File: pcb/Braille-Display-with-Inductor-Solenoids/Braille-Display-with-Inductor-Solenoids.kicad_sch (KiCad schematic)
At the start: 18 parts, among them J1 Screw_Terminal_01x02, J2 Screw_Terminal_01x02, J3 Screw_Terminal_01x02, SW1 SW_Push, SW2 SW_Push, U1 RP2040-Zero

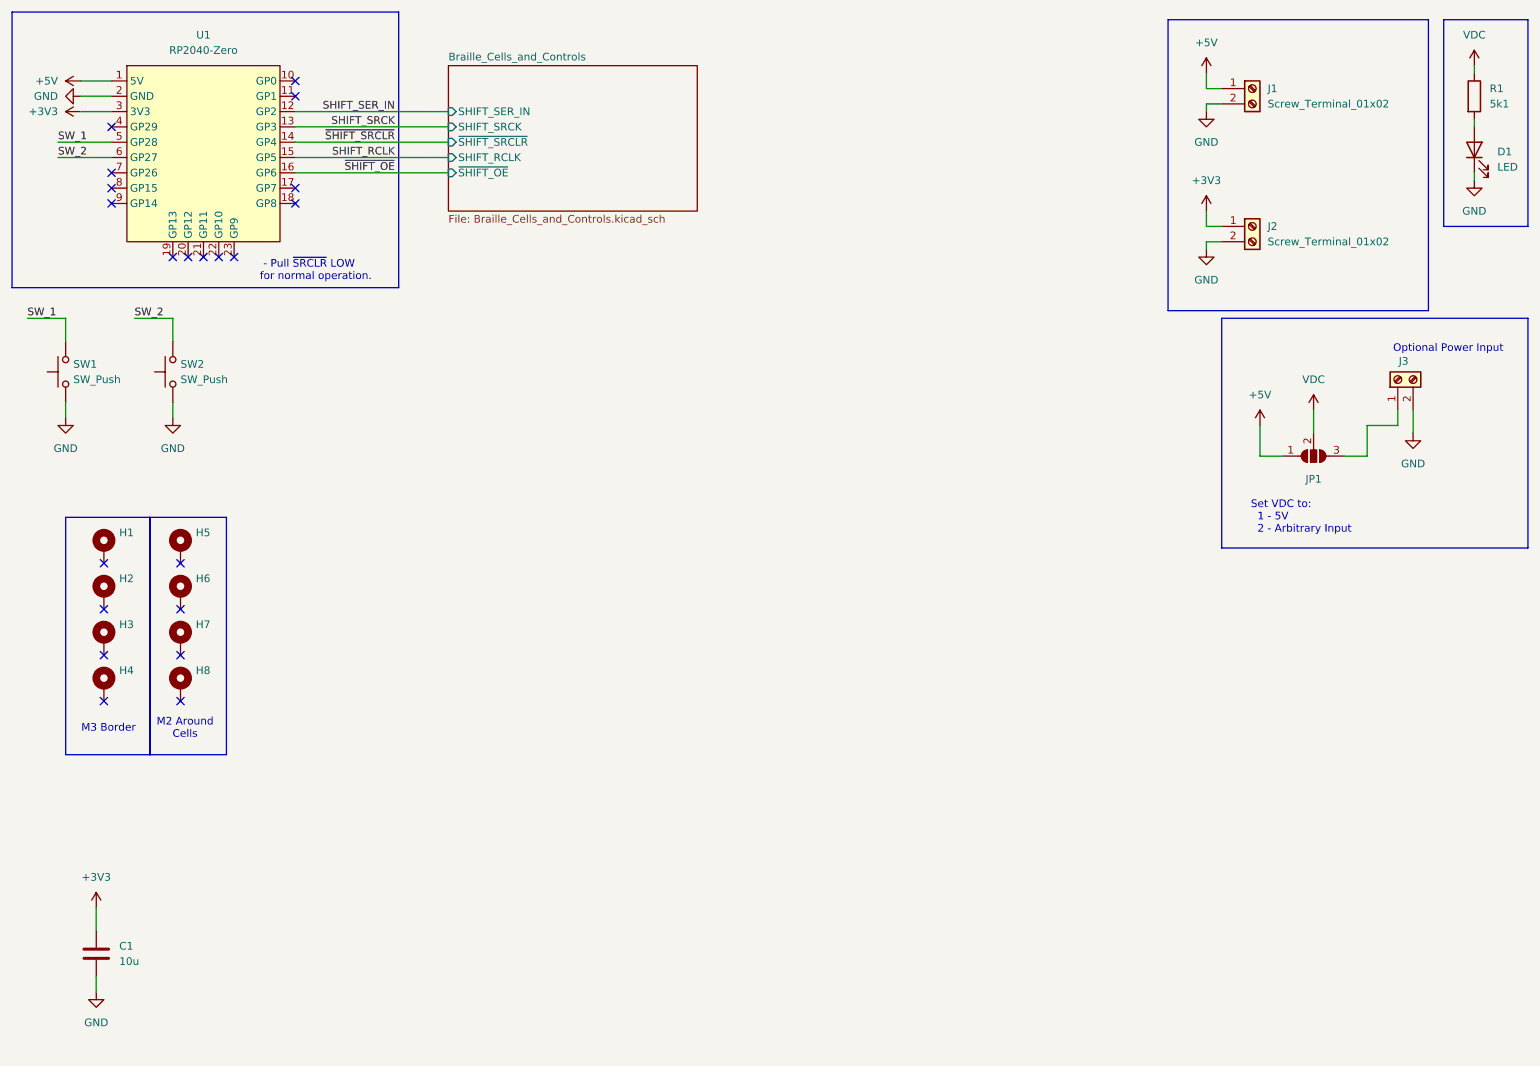
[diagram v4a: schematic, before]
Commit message: Layout debugging components
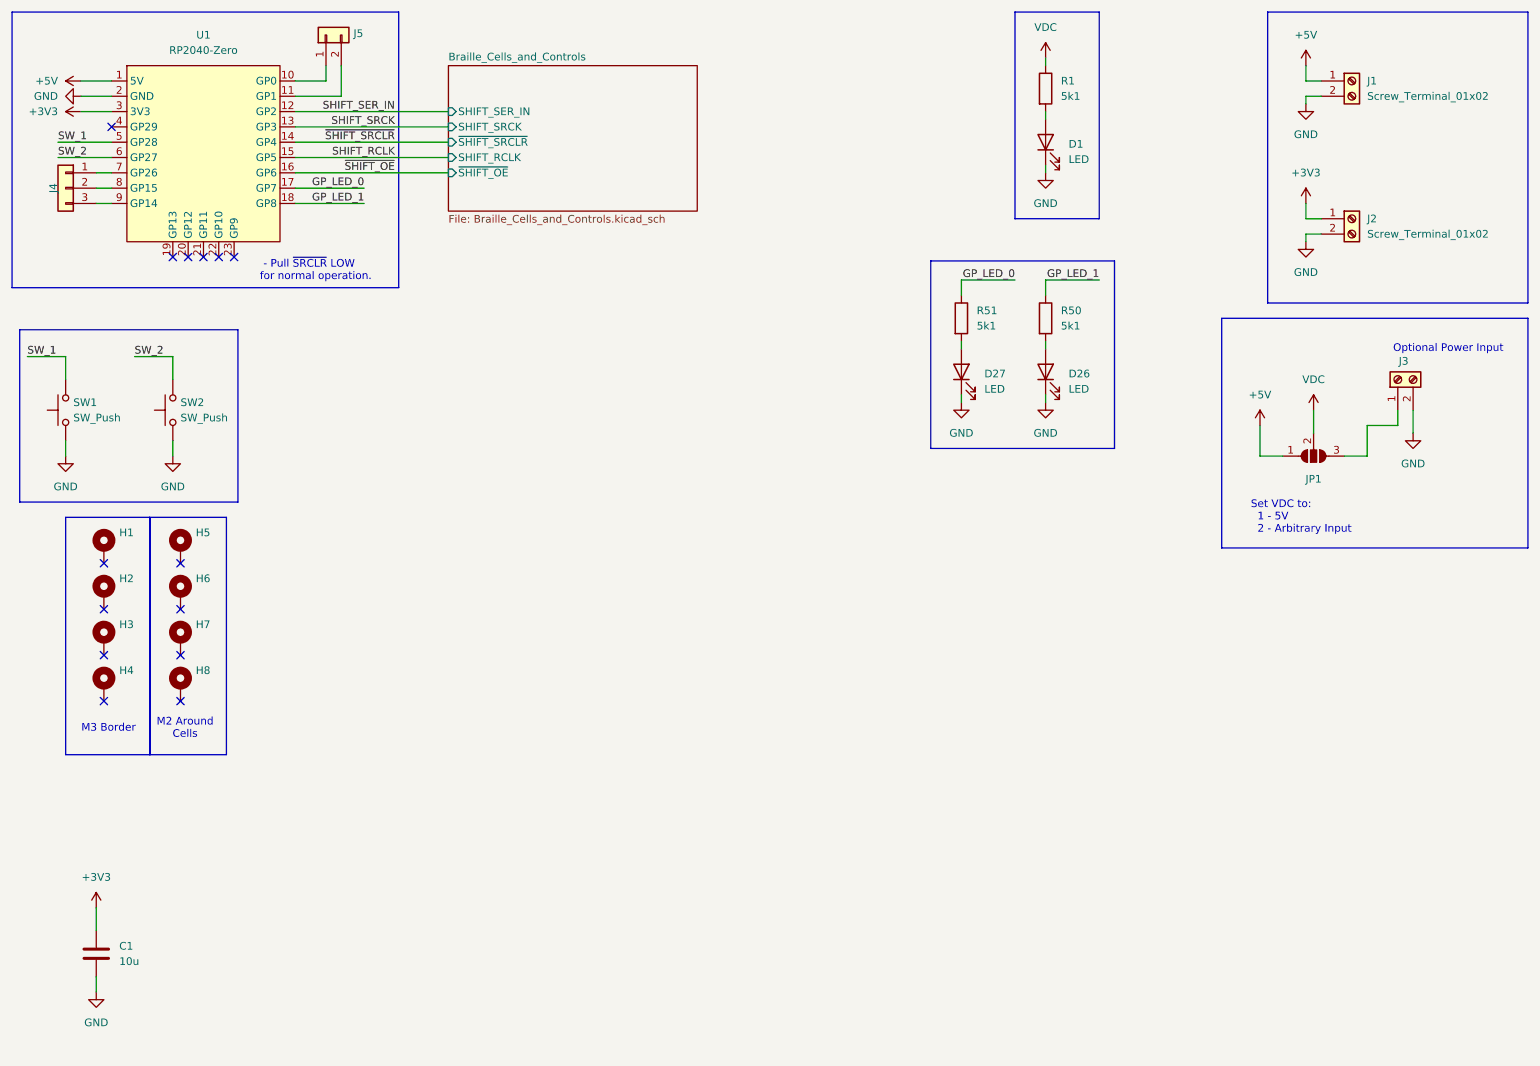
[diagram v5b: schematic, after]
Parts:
- added D26, D27: LED, LED_SMD:LED_1206_3216Metric_Pad1.42x1.75mm_HandSolder, symbol Device:LED
- added J4: Conn_01x03, Connector_PinHeader_2.54mm:PinHeader_1x03_P2.54mm_Vertical, symbol Connector_Generic:Conn_01x03
- added J5: Conn_01x02, Connector_PinHeader_2.54mm:PinHeader_1x02_P2.54mm_Vertical, symbol Connector_Generic:Conn_01x02
- added R50, R51: 5k1, Resistor_SMD:R_0603_1608Metric_Pad0.98x0.95mm_HandSolder, symbol Device:R
- R1: footprint Resistor_SMD:R_1206_3216Metric_Pad1.30x1.75mm_HandSolder -> Resistor_SMD:R_0603_1608Metric_Pad0.98x0.95mm_HandSolder
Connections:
- net GND: now also D26.1 (K), D27.1 (K)
- net at U1.10 (GP0): now also J5.1 (Pin_1)
- net at U1.11 (GP1): now also J5.2 (Pin_2)
- net GP_LED_0: now reaches U1.17 (GP7)
- net GP_LED_0: now also R51.1
- net GP_LED_1: now reaches U1.18 (GP8)
- net GP_LED_1: now also R50.1
- net at U1.7 (GP26): now also J4.1 (Pin_1)
- net at U1.8 (GP15): now also J4.2 (Pin_2)
- net at U1.9 (GP14): now also J4.3 (Pin_3)
- new net: D27.2 (A), R51.2
- new net: D26.2 (A), R50.2
- no-connect marks 21 -> 14
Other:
- moved on the sheet: D1, J1, J2, R1, SW1, SW2

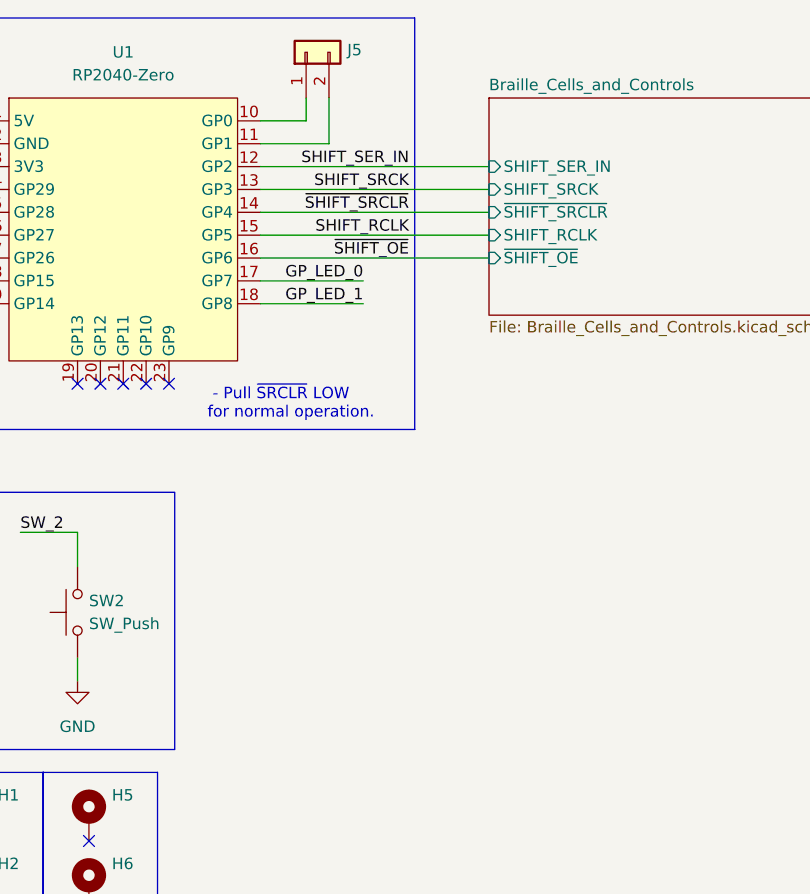
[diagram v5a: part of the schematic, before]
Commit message: Add UART soicbite
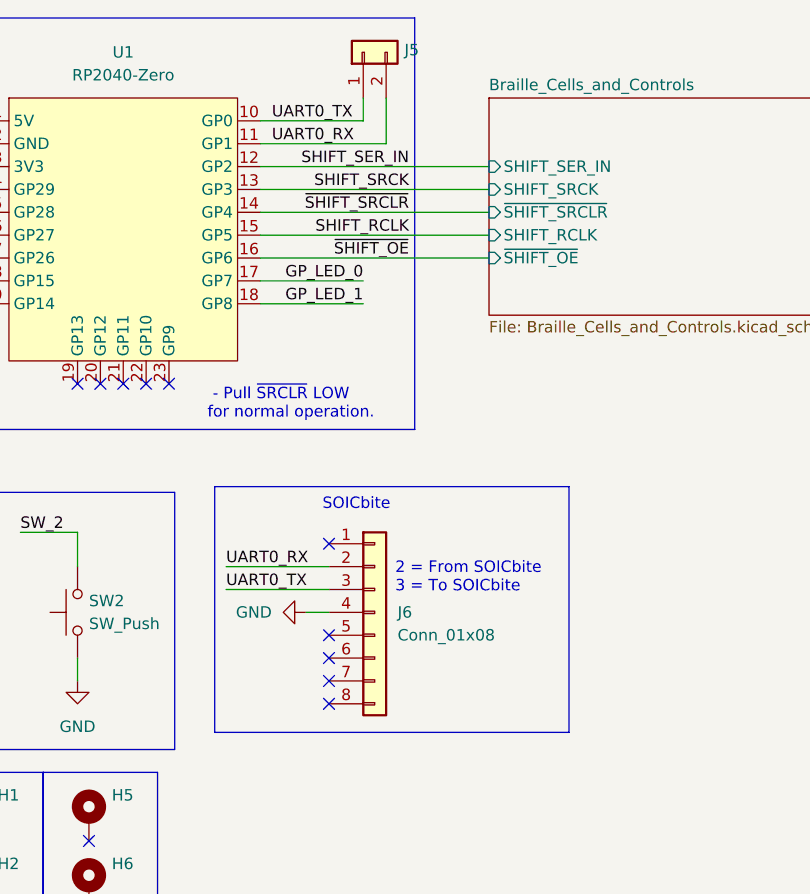
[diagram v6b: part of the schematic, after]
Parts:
- added J6: Conn_01x08, symbol Connector_Generic:Conn_01x08
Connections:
- net GND: now also J6.4 (Pin_4)
- net UART0_TX: now reaches J5.1 (Pin_1), U1.10 (GP0)
- net UART0_TX: now also J6.3 (Pin_3)
- net UART0_RX: now reaches J5.2 (Pin_2), U1.11 (GP1)
- net UART0_RX: now also J6.2 (Pin_2)
- no-connect marks 14 -> 19
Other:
- note added: "2 = From SOICbite 3 = To SOICbite"
- note added: "SOICbite"
- moved on the sheet: J5

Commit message: Layout SOICbite footprint
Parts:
- J6: footprint (none) -> 00-project-footprints:SOICbite_clipProgSmall
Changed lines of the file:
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@@
 			)
 		)
-		(property "Footprint" ""
+		(property "Footprint" "00-project-footprints:SOICbite_clipProgSmall"
 			(at 73.66 80.01 0)
 			(effects
